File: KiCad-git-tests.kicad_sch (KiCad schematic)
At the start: 0 parts

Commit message: New Demo Schematic
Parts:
- added D1: LED, symbol Device:LED
- added R1: R, Package_DIP:DIP-8_W7.62mm, symbol Device:R
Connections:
- new net: D1.2 (A), R1.2
- new net +5V: R1.1
- new net GND: D1.1 (K)
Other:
- note added: "Demo Schematic"

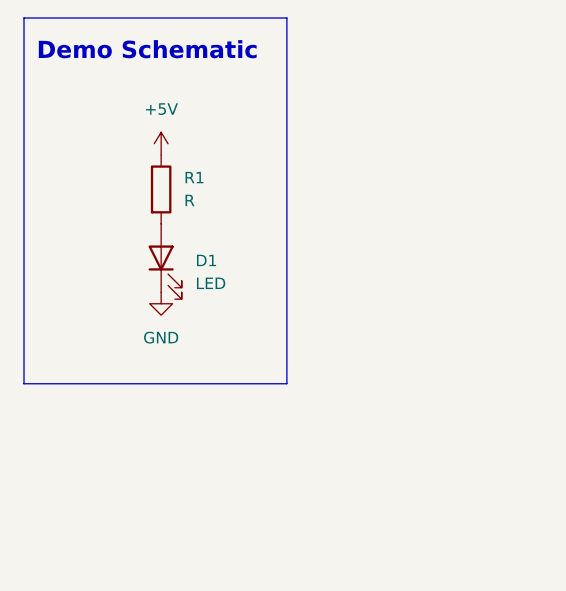
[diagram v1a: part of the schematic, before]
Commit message: Change the led and create a pcb
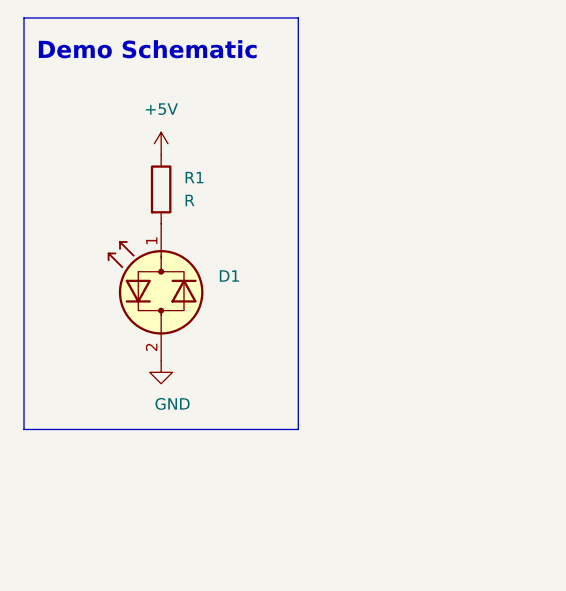
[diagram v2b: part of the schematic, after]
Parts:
- removed D1: LED, symbol Device:LED
- added D1: LED_Dual_Bidirectional, LED_SMD:LED_1812_4532Metric_Pad1.30x3.40mm_HandSolder, symbol Device:LED_Dual_Bidirectional
- R1: footprint Package_DIP:DIP-8_W7.62mm -> Resistor_SMD:R_0612_1632Metric
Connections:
- net GND: now also D1.2 (AK)
- net at R1.2: now also D1.1 (KA)
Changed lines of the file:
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@@
 	(rectangle
 		(start 59.69 19.05)
-		(end 88.9 59.69)
+		(end 90.17 64.77)
 		(stroke
 			(width 0)
@@
 	)
 	(symbol
-		(lib_id "Device:LED")
-		(at 74.93 45.72 90)
+		(lib_id "Device:LED_Dual_Bidirectional")
+		(at 74.93 49.53 90)
 		(unit 1)
 		(body_style 1)
@@
 		(fields_autoplaced yes)
 		(property "Reference" "D1"
-			(at 78.74 46.0374 90)
+			(at 81.28 47.7646 90)
 			(show_name no)
 			(do_not_autoplace no)
@@
 			)
 		)
-		(property "Value" "LED"
-			(at 78.74 48.5774 90)
+		(property "Value" "LED_Dual_Bidirectional"
+			(at 81.28 50.3046 90)
+			(hide yes)
 			(show_name no)
 			(do_not_autoplace no)
@@
 			)
 		)
-		(property "Footprint" ""
-			(at 74.93 45.72 0)
+		(property "Footprint" "LED_SMD:LED_1812_4532Metric_Pad1.30x3.40mm_HandSolder"
+			(at 74.93 49.53 0)
 			(hide yes)
 			(show_name no)
@@
 		)
 		(property "Datasheet" ""
-			(at 74.93 45.72 0)
-			(hide yes)
-			(show_name no)
-			(do_not_autoplace no)
-			(effects
-				(font
-					(size 1.27 1.27)
-				)
-			)
-		)
-		(property "Description" "Light emitting diode"
-			(at 74.93 45.72 0)
-			(hide yes)
-			(show_name no)
-			(do_not_autoplace no)
-			(effects
-				(font
-					(size 1.27 1.27)
-				)
-			)
-		)
-		(property "Sim.Pins" "1=K 2=A"
-			(at 74.93 45.72 0)
+			(at 74.93 49.53 0)
+			(hide yes)
+			(show_name no)
+			(do_not_autoplace no)
+			(effects
+				(font
+					(size 1.27 1.27)
+				)
+			)
+		)
+		(property "Description" "Dual LED, bidirectional"
+			(at 74.93 49.53 0)
 			(hide yes)
 			(show_name no)
@@
 	(symbol
 		(lib_id "power:GND")
-		(at 74.93 49.53 0)
-		(unit 1)
-		(body_style 1)
-		(exclude_from_sim no)
-		(in_bom yes)
-		(on_board yes)
-		(in_pos_files yes)
-		(dnp no)
-		(fields_autoplaced yes)
+		(at 74.93 57.15 0)
+		(unit 1)
+		(body_style 1)
+		(exclude_from_sim no)
+		(in_bom yes)
+		(on_board yes)
+		(in_pos_files yes)
+		(dnp no)
 		(property "Reference" "#PWR02"
-			(at 74.93 55.88 0)
+			(at 74.93 63.5 0)
 			(hide yes)
 			(show_name no)
@@
 		)
 		(property "Value" "GND"
-			(at 74.93 54.61 0)
+			(at 76.2 61.976 0)
 			(show_name no)
 			(do_not_autoplace no)
@@
 		)
 		(property "Footprint" ""
-			(at 74.93 49.53 0)
+			(at 74.93 57.15 0)
 			(hide yes)
 			(show_name no)
@@
 		)
 		(property "Datasheet" ""
-			(at 74.93 49.53 0)
+			(at 74.93 57.15 0)
 			(hide yes)
 			(show_name no)
@@
 		)
 		(property "Description" "Power symbol creates a global label with name \"GND\" , ground"
-			(at 74.93 49.53 0)
+			(at 74.93 57.15 0)
 			(hide yes)
 			(show_name no)
@@
 			)
 		)
-		(property "Footprint" "Package_DIP:DIP-8_W7.62mm"
+		(property "Footprint" "Resistor_SMD:R_0612_1632Metric"
 			(at 73.152 38.1 90)
 			(hide yes)

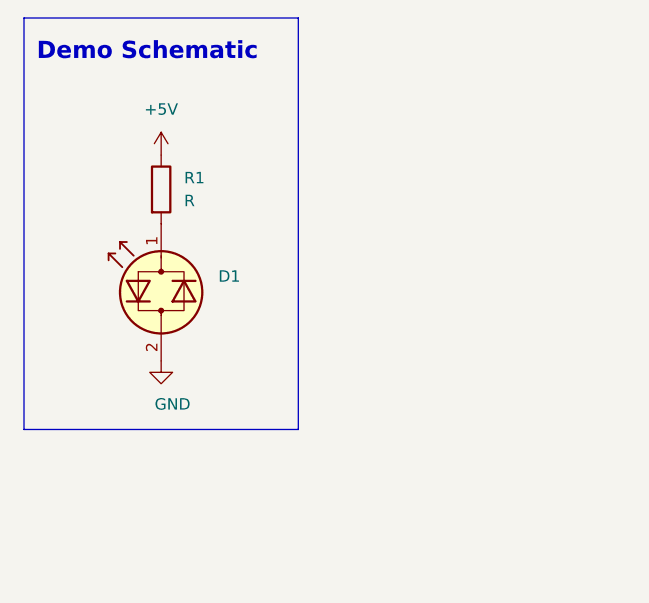
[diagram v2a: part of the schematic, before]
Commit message: Flip led to test KiRi
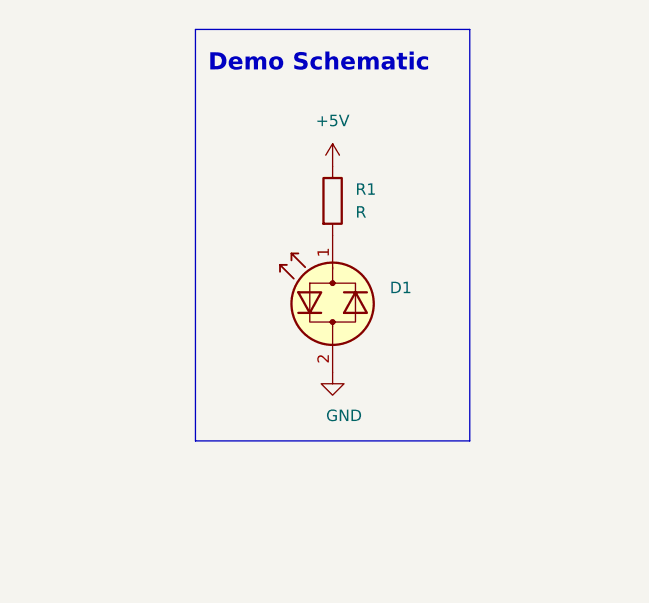
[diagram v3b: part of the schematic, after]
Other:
- moved on the sheet: D1, R1
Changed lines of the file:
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@@
 	)
 	(rectangle
-		(start 59.69 19.05)
-		(end 90.17 64.77)
+		(start 78.74 20.32)
+		(end 109.22 66.04)
 		(stroke
 			(width 0)
@@
 	(text "Demo Schematic\n"
 		(exclude_from_sim no)
-		(at 73.406 22.86 0)
+		(at 92.456 24.13 0)
 		(effects
 			(font
@@
 	(symbol
 		(lib_id "Device:LED_Dual_Bidirectional")
-		(at 74.93 49.53 90)
+		(at 93.98 50.8 90)
 		(unit 1)
 		(body_style 1)
@@
 		(fields_autoplaced yes)
 		(property "Reference" "D1"
-			(at 81.28 47.7646 90)
+			(at 100.33 49.0346 90)
 			(show_name no)
 			(do_not_autoplace no)
@@
 		)
 		(property "Value" "LED_Dual_Bidirectional"
-			(at 81.28 50.3046 90)
+			(at 100.33 51.5746 90)
 			(hide yes)
 			(show_name no)
@@
 		)
 		(property "Footprint" "LED_SMD:LED_1812_4532Metric_Pad1.30x3.40mm_HandSolder"
-			(at 74.93 49.53 0)
+			(at 93.98 50.8 0)
 			(hide yes)
 			(show_name no)
@@
 		)
 		(property "Datasheet" ""
-			(at 74.93 49.53 0)
+			(at 93.98 50.8 0)
 			(hide yes)
 			(show_name no)
@@
 		)
 		(property "Description" "Dual LED, bidirectional"
-			(at 74.93 49.53 0)
+			(at 93.98 50.8 0)
 			(hide yes)
 			(show_name no)
@@
 	(symbol
 		(lib_id "power:+5V")
-		(at 74.93 34.29 0)
+		(at 93.98 35.56 0)
 		(unit 1)
 		(body_style 1)
@@
 		(fields_autoplaced yes)
 		(property "Reference" "#PWR01"
-			(at 74.93 38.1 0)
+			(at 93.98 39.37 0)
 			(hide yes)
 			(show_name no)
@@
 		)
 		(property "Value" "+5V"
-			(at 74.93 29.21 0)
+			(at 93.98 30.48 0)
 			(show_name no)
 			(do_not_autoplace no)
@@
 		)
 		(property "Footprint" "Converter_ACDC:Converter_ACDC_Vigortronix_VTX-214-010-1xx_THT"
-			(at 74.93 34.29 0)
+			(at 93.98 35.56 0)
 			(hide yes)
 			(show_name no)
@@
 		)
 		(property "Datasheet" ""
-			(at 74.93 34.29 0)
+			(at 93.98 35.56 0)
 			(hide yes)
 			(show_name no)
@@
 		)
 		(property "Description" "Power symbol creates a global label with name \"+5V\""
-			(at 74.93 34.29 0)
+			(at 93.98 35.56 0)
 			(hide yes)
 			(show_name no)
@@
 	(symbol
 		(lib_id "power:GND")
-		(at 74.93 57.15 0)
+		(at 93.98 58.42 0)
 		(unit 1)
 		(body_style 1)
@@
 		(dnp no)
 		(property "Reference" "#PWR02"
-			(at 74.93 63.5 0)
+			(at 93.98 64.77 0)
 			(hide yes)
 			(show_name no)
@@
 		)
 		(property "Value" "GND"
-			(at 76.2 61.976 0)
+			(at 95.25 63.246 0)
 			(show_name no)
 			(do_not_autoplace no)
@@
 		)
 		(property "Footprint" ""
-			(at 74.93 57.15 0)
+			(at 93.98 58.42 0)
 			(hide yes)
 			(show_name no)
@@
 		)
 		(property "Datasheet" ""
-			(at 74.93 57.15 0)
+			(at 93.98 58.42 0)
 			(hide yes)
 			(show_name no)
@@
 		)
 		(property "Description" "Power symbol creates a global label with name \"GND\" , ground"
-			(at 74.93 57.15 0)
+			(at 93.98 58.42 0)
 			(hide yes)
 			(show_name no)
@@
 	(symbol
 		(lib_id "Device:R")
-		(at 74.93 38.1 0)
+		(at 93.98 39.37 0)
 		(unit 1)
 		(body_style 1)
@@
 		(fields_autoplaced yes)
 		(property "Reference" "R1"
-			(at 77.47 36.8299 0)
+			(at 96.52 38.0999 0)
 			(show_name no)
 			(do_not_autoplace no)
@@
 		)
 		(property "Value" "R"
-			(at 77.47 39.3699 0)
+			(at 96.52 40.6399 0)
 			(show_name no)
 			(do_not_autoplace no)
@@
 		)
 		(property "Footprint" "Resistor_SMD:R_0612_1632Metric"
-			(at 73.152 38.1 90)
+			(at 92.202 39.37 90)
 			(hide yes)
 			(show_name no)
@@
 		)
 		(property "Datasheet" ""
-			(at 74.93 38.1 0)
+			(at 93.98 39.37 0)
 			(hide yes)
 			(show_name no)
@@
 		)
 		(property "Description" "Resistor"
-			(at 74.93 38.1 0)
-			(hide yes)
-			(show_name no)
+			(at 93.98 39.37 0)
+			(hide yes)
+			(show_name no)

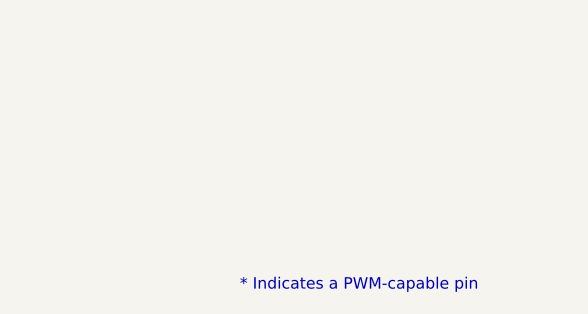
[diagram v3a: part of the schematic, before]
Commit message: Fix template problem
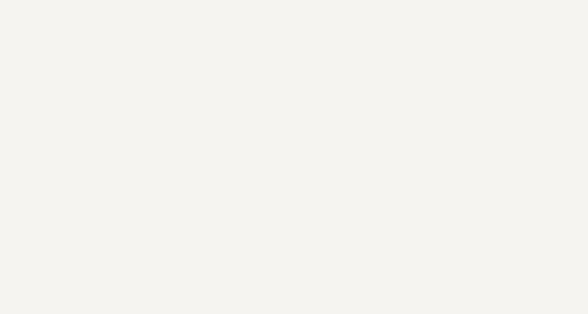
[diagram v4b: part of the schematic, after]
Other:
- note removed: "* Indicates a PWM-capable pin"
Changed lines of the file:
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@@
 	(paper "A4")
 	(title_block
-		(date "mar. 31 mars 2015")
+		(date "2026-09-15")
 	)
 	(rectangle
@@
 		)
 	)
-	(text "* Indicates a PWM-capable pin"
-		(exclude_from_sim no)
-		(at 177.8 180.34 0)
-		(effects
-			(font
-				(size 1.27 1.27)
-			)
-			(justify left bottom)
-		)
-	)
